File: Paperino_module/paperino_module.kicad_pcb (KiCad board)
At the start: 2 copper layers, 25.4 x 22 mm, 21 parts, among them P1 CONN_01X06, P2 CONN_01X06, P3 CONN_01X06, P4 CONN_01X06, Q1 PMOS, Q2 NMOS, U1 BMA250E, X1 XF2M-2615-1A, X2 XF2B-4545-1A

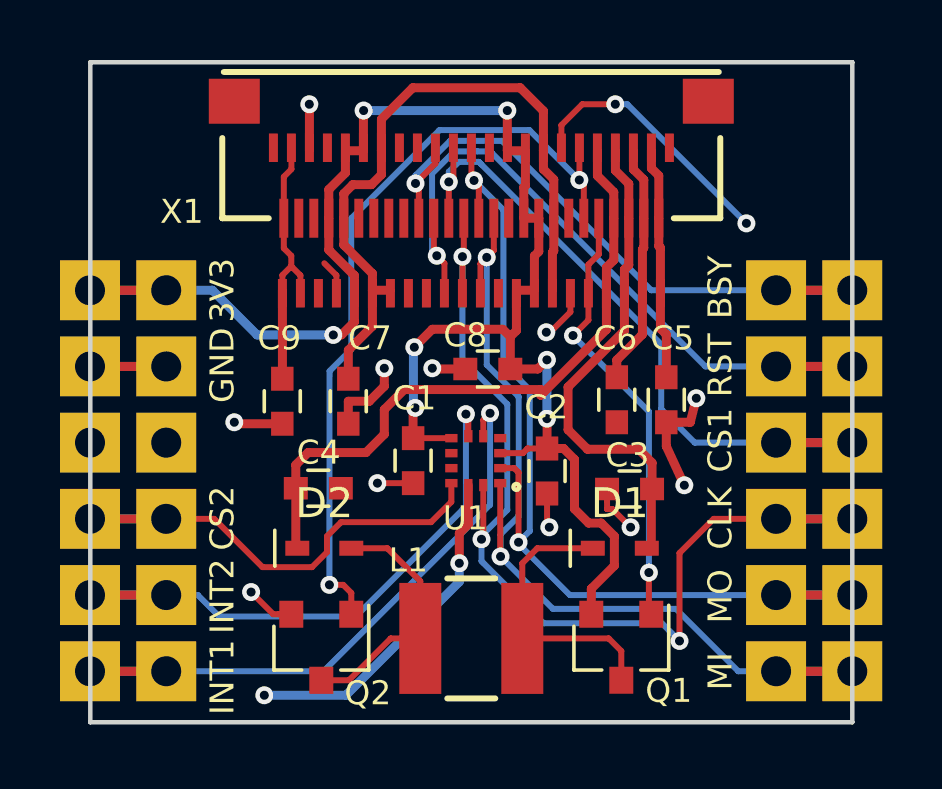
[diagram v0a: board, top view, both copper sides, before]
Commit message: flipped connector on module
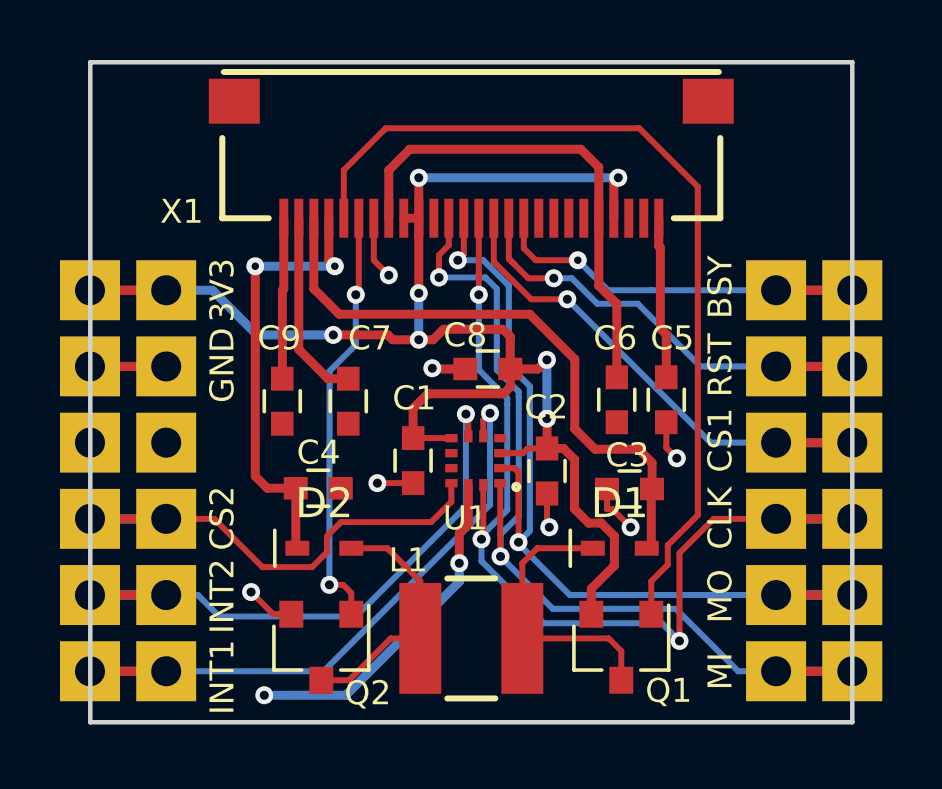
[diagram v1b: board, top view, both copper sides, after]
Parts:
- removed X2: XF2B-4545-1A, Paperino:XF2B-4545-31A
- C5: value 1µ -> 100n
- C9: value 100n -> 1µ
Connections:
- C5 pad 1: /VSL -> /TPCOM
- C6 pad 1: /VSH -> /VDD
- C7 pad 1: /VDD -> /VSH
- C9 pad 1: /TPCOM -> /VSL
- X1 pad 1: /VSL -> /TPCOM
- X1 pad 10: +3V3 -> /~BUSY
- X1 pad 11: Net-(X1-Pad11) -> /~RST
- X1 pad 12: /SPI_MISO -> /SPI_CS1
- X1 pad 13: /SPI_MOSI -> /SPI_CLK
- X1 pad 14: /SPI_CLK -> /SPI_MOSI
- X1 pad 15: /SPI_CS1 -> /SPI_MISO
- X1 pad 16: /~RST -> Net-(X1-Pad16)
- X1 pad 17: /~BUSY -> +3V3
- X1 pad 18: Net-(X1-Pad18) -> +3V3
- X1 pad 19: Net-(X1-Pad19) -> /VDD
- X1 pad 2: /VSH -> GND
- X1 pad 20: Net-(X1-Pad20) -> GND
- X1 pad 21: Net-(X1-Pad21) -> /GDR_N
- X1 pad 22: /VDD -> /GDR_P
- X1 pad 23: +3V3 -> /VGH
- X1 pad 24: GND -> /VGL
- X1 pad 25: GND -> /VSH
- X1 pad 26: /TPCOM -> /VSL
- X1 pad 3: /VGL -> GND
- X1 pad 4: /VGH -> +3V3
- X1 pad 5: /GDR_P -> /VDD
- X1 pad 6: /GDR_N -> Net-(X1-Pad6)
- X1 pad 7: GND -> Net-(X1-Pad7)
- X1 pad 8: /VDD -> Net-(X1-Pad8)
- X1 pad 9: +3V3 -> Net-(X1-Pad9)
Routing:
- net GND: track 45.7 -> 27.6 mm, vias 15 -> 9
- net /GDR_P: track 14.6 -> 29.8 mm, vias 2 -> 0
- net /GDR_N: track 25.9 -> 14.2 mm
- net /~RST: track 25.2 -> 17.0 mm
- net /~BUSY: track 22.5 -> 15.1 mm
- net /VGH: track 22.1 -> 14.9 mm, vias 0 -> 2
- net /VDD: track 23.2 -> 16.4 mm
- net /SPI_CS1: track 23.9 -> 18.4 mm
- net +3V3: track 56.9 -> 52.2 mm
- net /VGL: track 16.4 -> 20.2 mm
- net /TPCOM: track 8.86 -> 5.18 mm
- net /SPI_MOSI: track 32.8 -> 29.9 mm
- net /VSL: track 7.53 -> 5.37 mm
- net /VSH: track 7.84 -> 6.43 mm
- net /SPI_CLK: track 34.8 -> 33.5 mm
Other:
- net class Default: via_drill 0.25 -> 0.3

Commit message: stitching via
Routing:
- net GND: track 27.6 -> 33.5 mm, vias 9 -> 10
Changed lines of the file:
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@@
     (thickness 1.6)
     (drawings 15)
-    (tracks 285)
+    (tracks 289)
     (zones 0)
     (modules 20)
@@
   (segment (start 137.12 97.13) (end 137.275 96.975) (width 0.2) (layer F.Cu) (net 1))
   (segment (start 134.735 96.63) (end 133.46 96.63) (width 0.2) (layer F.Cu) (net 1) (status 30))
+  (segment (start 126.81 94.24) (end 127.175 93.875) (width 0.2) (layer F.Cu) (net 2))
+  (segment (start 127.175 93.875) (end 127.175 90.1) (width 0.2) (layer F.Cu) (net 2))
+  (via (at 127.175 90.1) (size 0.6) (drill 0.3) (layers F.Cu B.Cu) (net 2))
+  (segment (start 125.23 94.24) (end 126.81 94.24) (width 0.2) (layer F.Cu) (net 2))
   (segment (start 141.9 96.1) (end 141.9 96.95) (width 0.2) (layer F.Cu) (net 2))
   (via (at 142.25 97.3) (size 0.6) (drill 0.3) (layers F.Cu B.Cu) (net 2))
@@
   (segment (start 128.2 90.9) (end 128.2 97.9) (width 0.3) (layer F.Cu) (net 4))
   (segment (start 130.65 90.7) (end 130.85 90.9) (width 0.3) (layer F.Cu) (net 4))
-  (via (at 130.85 90.9) (size 0.6) (drill 0.25) (layers F.Cu B.Cu) (net 4))
+  (via (at 130.85 90.9) (size 0.6) (drill 0.3) (layers F.Cu B.Cu) (net 4))
   (segment (start 130.85 90.9) (end 128.2 90.9) (width 0.3) (layer B.Cu) (net 4))
-  (via (at 128.2 90.9) (size 0.6) (drill 0.25) (layers F.Cu B.Cu) (net 4))
+  (via (at 128.2 90.9) (size 0.6) (drill 0.3) (layers F.Cu B.Cu) (net 4))
   (segment (start 130.65 89.3) (end 130.65 90.7) (width 0.3) (layer F.Cu) (net 4))
   (segment (start 128.6 98.3) (end 129.55 98.3) (width 0.3) (layer F.Cu) (net 4))
@@
   (segment (start 137.55 90.7) (end 137.15 90.3) (width 0.2) (layer F.Cu) (net 16))
   (segment (start 138.95 90.7) (end 137.55 90.7) (width 0.2) (layer F.Cu) (net 16))
-  (via (at 138.95 90.7) (size 0.6) (drill 0.25) (layers F.Cu B.Cu) (net 16))
+  (via (at 138.95 90.7) (size 0.6) (drill 0.3) (layers F.Cu B.Cu) (net 16))
   (segment (start 139.95 91.7) (end 138.95 90.7) (width 0.2) (layer B.Cu) (net 16))
   (segment (start 145.56 91.7) (end 148.1 91.7) (width 0.3) (layer B.Cu) (net 16) (status 30))
